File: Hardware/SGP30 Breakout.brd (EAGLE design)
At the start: 25.4 x 25.4 mm, 45 parts, among them J3 PTH, U1 SGP30, U2 AP2112K

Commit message: pre-review changes
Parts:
- removed J3: PTH, SparkX:1X04_NO_SILK
- added I2C: JUMPER-SMT_3_2-NC_TRACE_SILK, SparkFun-Jumpers:SMT-JUMPER_3_2-NC_TRACE_SILK
- added J1: (no value), SparkFun-Connectors:1X04_NO_SILK
- added U$14: (no value), buzzard_labels (4):ADR#_0X580
- added U$15: (no value), SparkFun-Buzzard:I2C
- added U$16: (no value), SparkFun-Aesthetics:QWIIC_5MM
- J2, J4: value (none) -> QWIIC_RIGHT_ANGLE; device SparkFun-Connectors:1X04_1MM_RA -> SparkFun-Connectors:JST04_1MM_RA
- Q1, Q2: value (none) -> 220mA/50V/3.5Ω
- renumbered U1 to U3
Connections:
- new net N$2: I2C.3, R1.2
- new net N$4: I2C.1, R7.2
- net 3.3V: now also I2C.2, J1.2; no longer J3.2, R1.2, R7.2
- net GND: now also J1.1; no longer J3.1
- net SCL: now also J1.4; no longer J3.4
- net SDA: now also J1.3; no longer J3.3
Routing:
- net N$4: track 0.00 -> 5.81 mm, vias 0 -> 1
- net N$2: track 0.00 -> 5.80 mm, vias 0 -> 1
- net GND: track 5.38 -> 1.85 mm, vias 10 -> 13
- net N$1: track 0.00 -> 1.99 mm
- net 3.3V: track 65.5 -> 66.7 mm, vias 2 -> 3

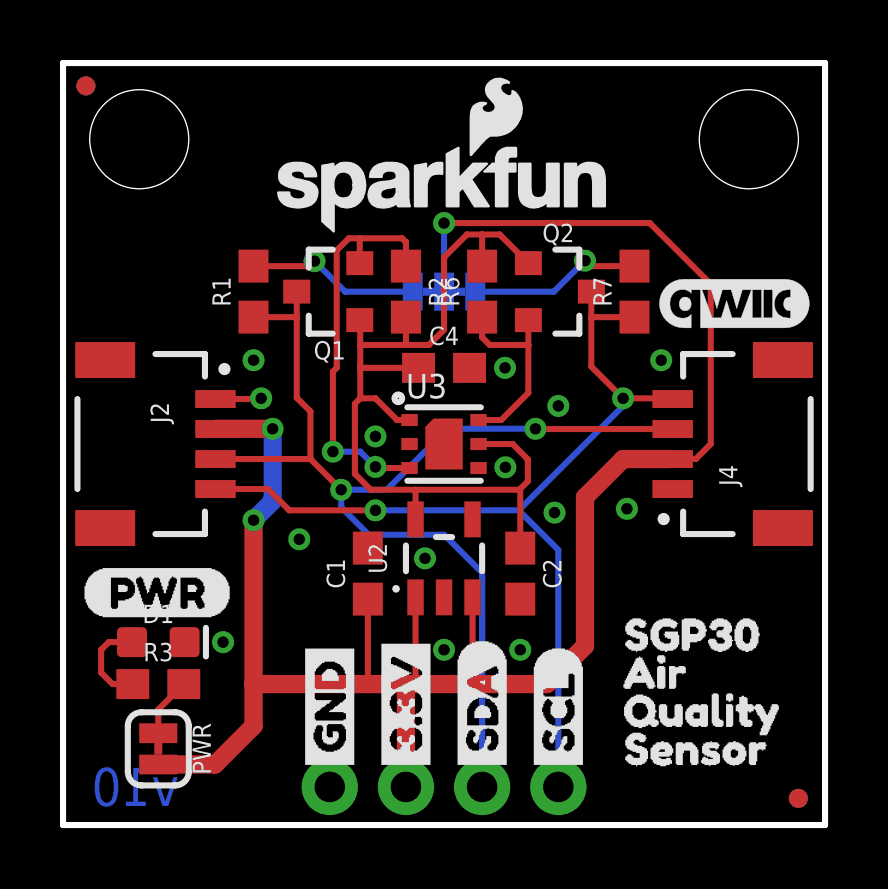
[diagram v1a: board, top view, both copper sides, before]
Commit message: Post review/checklist changes
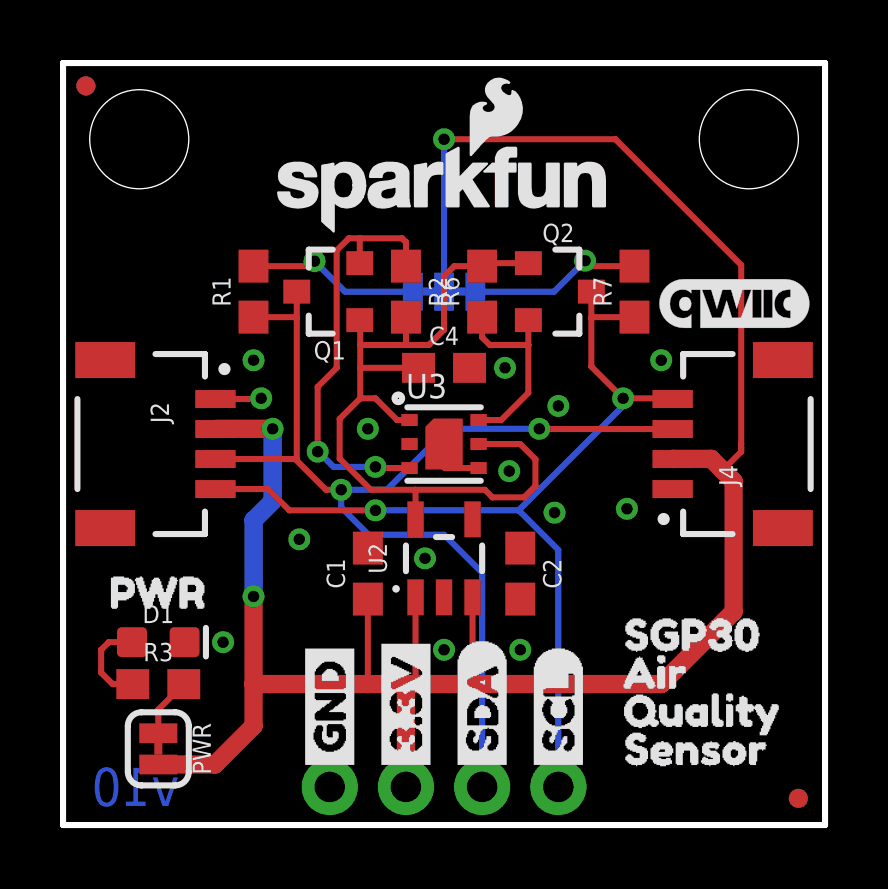
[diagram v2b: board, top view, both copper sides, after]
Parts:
- removed U$10: (no value), Labels-0_04:(PWR)
- added U$17: (no value), SparkFun-Buzzard:PWR_TO
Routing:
- net 3.3V: track 66.7 -> 75.5 mm
- net 1.8V: track 31.7 -> 28.7 mm
- net GND: track 1.85 -> 3.78 mm, vias 13 -> 14
- net LSDA: track 13.7 -> 14.4 mm

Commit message: post qc-double check
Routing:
- net 1.8V: track 28.7 -> 30.5 mm
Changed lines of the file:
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@@
 <wire x1="13.97" y1="18.63" x2="14.07" y2="18.73" width="0.2032" layer="1"/>
 <wire x1="14.07" y1="18.73" x2="15.51" y2="18.73" width="0.2032" layer="1"/>
-<wire x1="15.748" y1="11.303" x2="15.367" y2="10.922" width="0.2032" layer="1"/>
+<wire x1="15.748" y1="11.176" x2="15.494" y2="10.922" width="0.2032" layer="1"/>
 <wire x1="14.31523125" y1="10.922" x2="14.06123125" y2="11.176" width="0.2032" layer="1"/>
 <wire x1="14.06123125" y1="11.176" x2="11.75" y2="11.176" width="0.2032" layer="1"/>
-<wire x1="15.748" y1="12.192" x2="15.748" y2="11.303" width="0.2032" layer="1"/>
-<wire x1="15.367" y1="10.922" x2="14.31523125" y2="10.922" width="0.2032" layer="1"/>
-<wire x1="11.75" y1="10.1901" x2="15.24" y2="9.232" width="0" layer="19" extent="1-1"/>
+<wire x1="15.748" y1="12.192" x2="15.748" y2="11.176" width="0.2032" layer="1"/>
+<wire x1="15.494" y1="10.922" x2="15.24" y2="10.922" width="0.2032" layer="1"/>
+<wire x1="15.24" y1="10.922" x2="14.31523125" y2="10.922" width="0.2032" layer="1"/>
+<wire x1="15.24" y1="9.232" x2="15.24" y2="10.922" width="0.1778" layer="1"/>
 </signal>
 <signal name="LSDA">
